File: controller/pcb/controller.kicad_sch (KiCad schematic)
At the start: 22 parts, among them SW1 SW_Push, SW2 SW_Push, SW3 SW_Push, SW4 SW_Push, U1 COM-09032, U2 COM-09032, U3 NRF24L01_Breakout, U4 ESP32C3-SUPERMINI, U5 74HC148

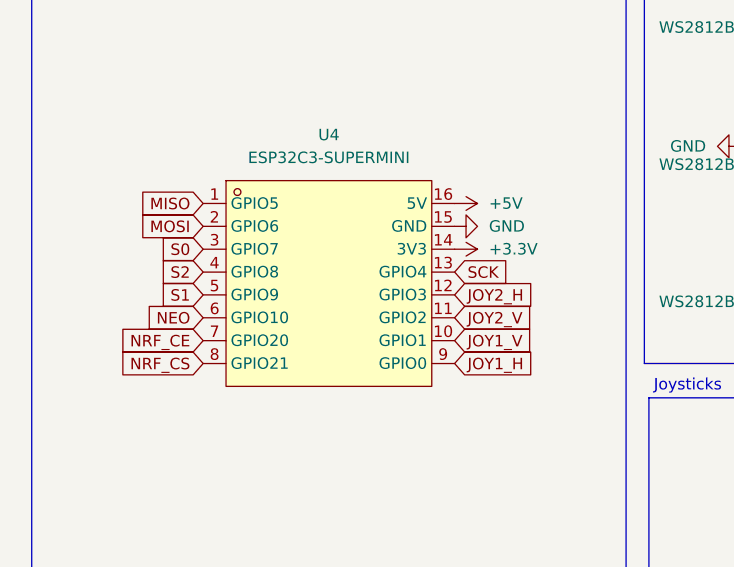
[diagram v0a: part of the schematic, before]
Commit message: [firmware] add v202 protocl and nrf24 driver code
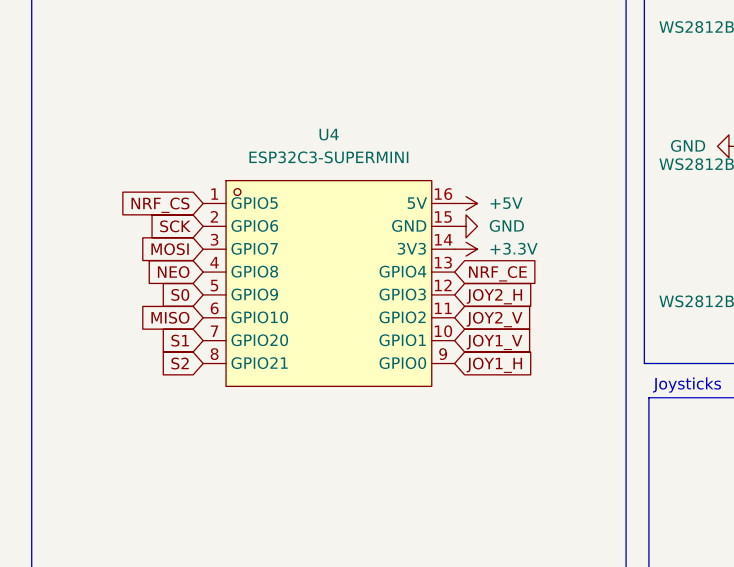
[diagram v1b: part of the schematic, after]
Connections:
- net MISO: now also U4.6 (GPIO10); no longer U4.1 (GPIO5)
- net MOSI: now also U4.3 (GPIO7); no longer U4.2 (GPIO6)
- net NEO: now also U4.4 (GPIO8); no longer U4.6 (GPIO10)
- net NRF_CE: now also U4.13 (GPIO4); no longer U4.7 (GPIO20)
- net NRF_CS: now also U4.1 (GPIO5); no longer U4.8 (GPIO21)
- net S0: now also U4.5 (GPIO9); no longer U4.3 (GPIO7)
- net S1: now also U4.7 (GPIO20); no longer U4.5 (GPIO9)
- net S2: now also U4.8 (GPIO21); no longer U4.4 (GPIO8)
- net SCK: now also U4.2 (GPIO6); no longer U4.13 (GPIO4)

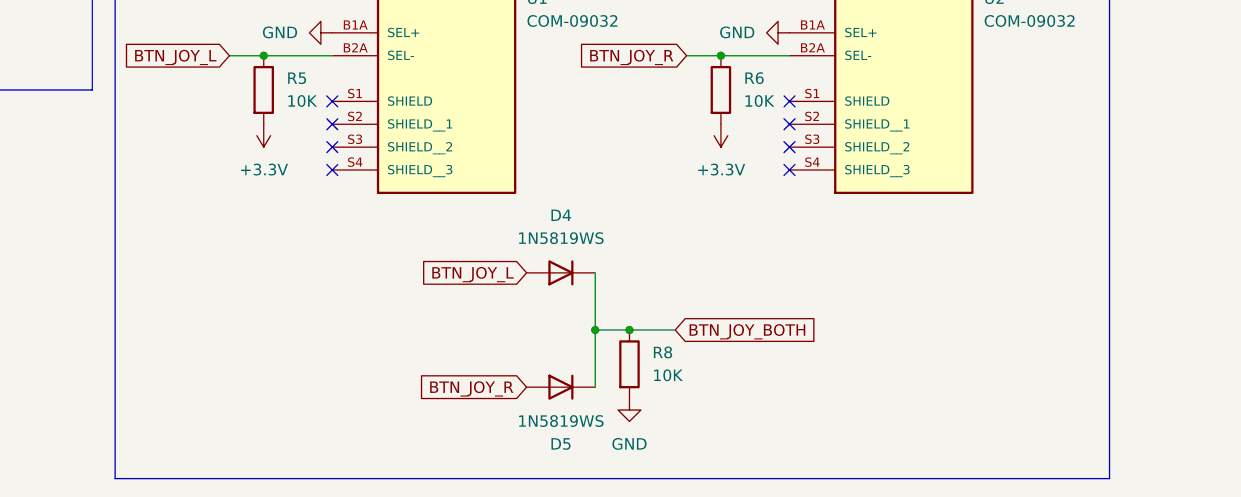
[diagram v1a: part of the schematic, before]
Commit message: [controller] add smoothing caps to ADC lines
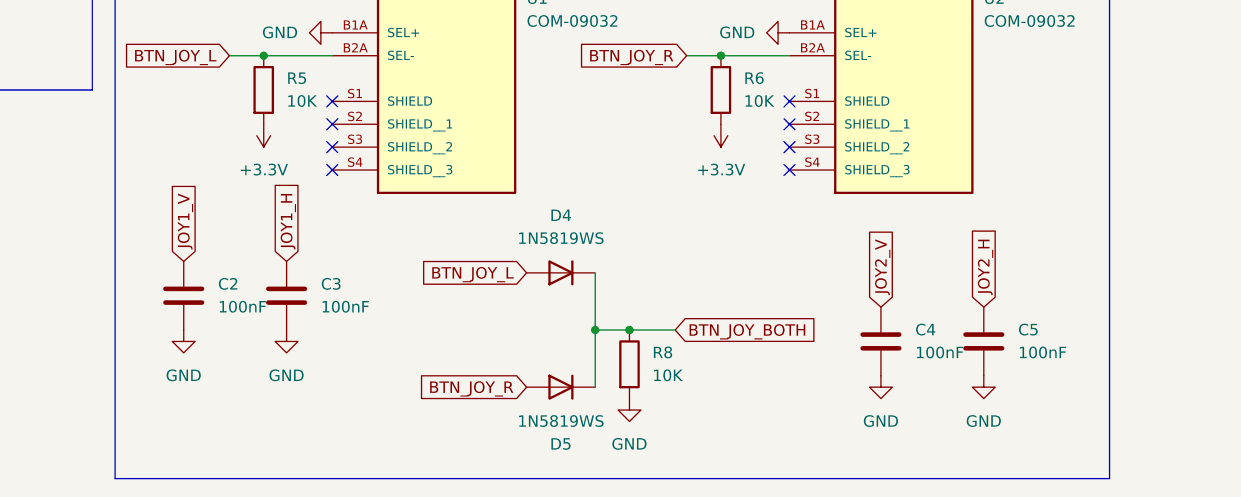
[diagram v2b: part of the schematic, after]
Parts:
- added C2, C3, C4, C5: 100nF, Capacitor_SMD:C_0805_2012Metric, symbol Device:C
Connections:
- net GND: now also C2.2, C3.2, C4.2, C5.2
- net JOY1_H: now also C3.1
- net JOY1_V: now also C2.1
- net JOY2_H: now also C5.1
- net JOY2_V: now also C4.1

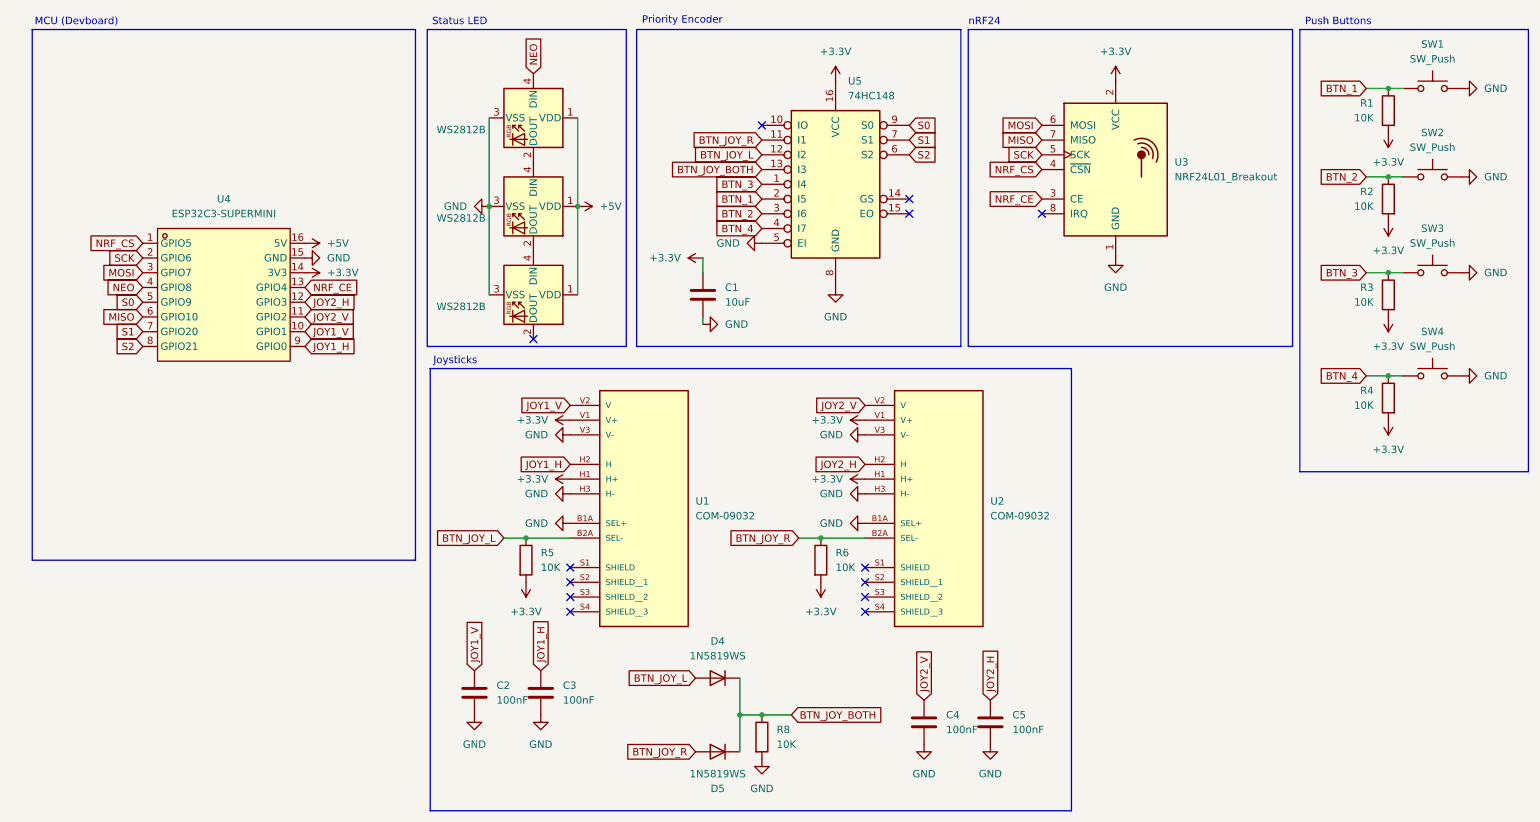
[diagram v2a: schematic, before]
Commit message: [controller] use higher quality external ADC
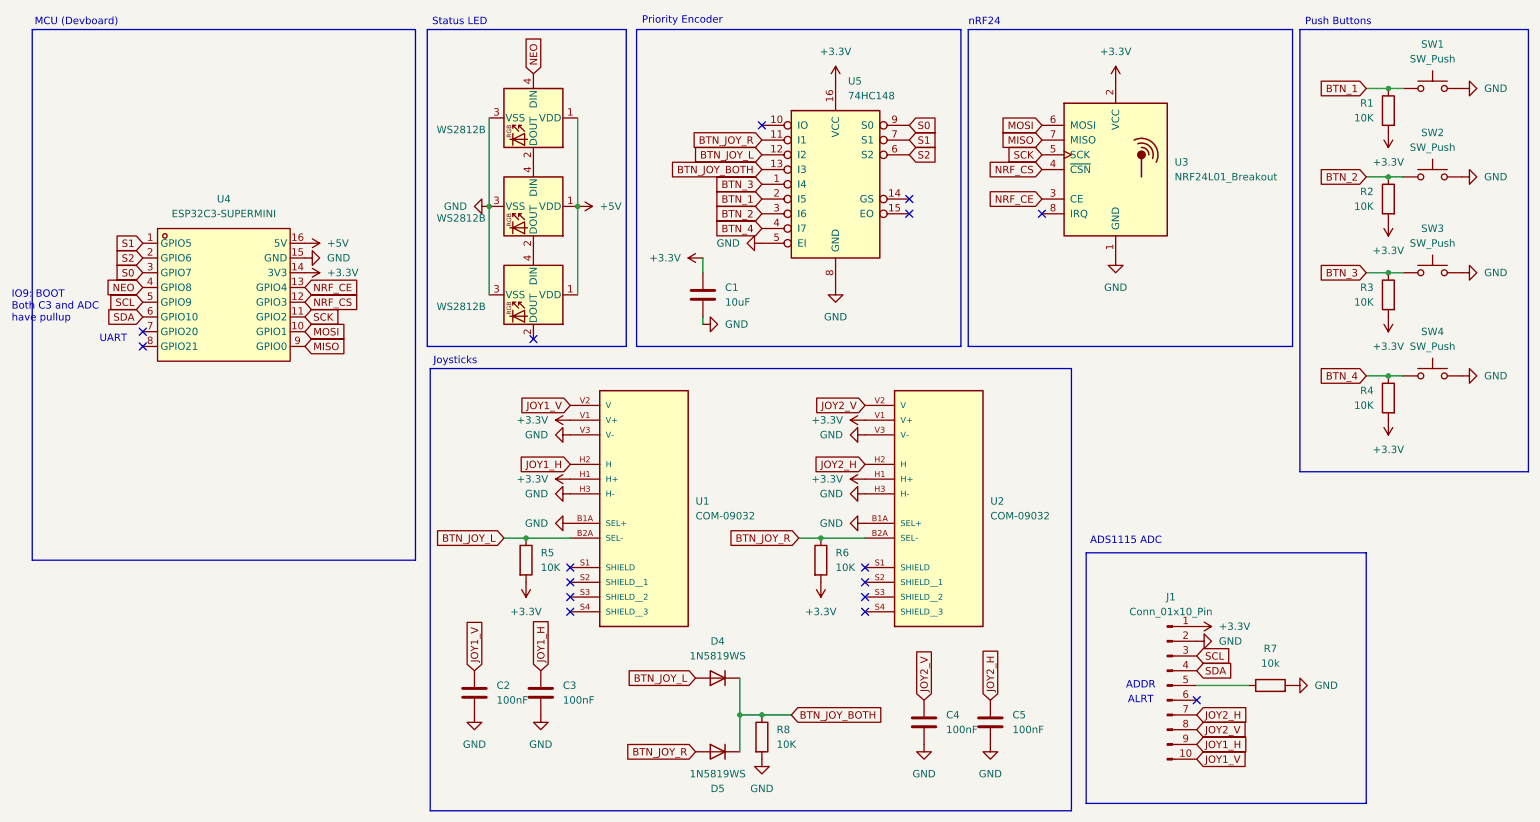
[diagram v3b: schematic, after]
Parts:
- added J1: Conn_01x10_Pin, Connector_PinHeader_2.54mm:PinHeader_1x10_P2.54mm_Vertical, symbol Connector:Conn_01x10_Pin
- added R7: 10k, Resistor_SMD:R_0805_2012Metric, symbol Device:R
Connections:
- net +3.3V: now also J1.1 (Pin_1)
- net GND: now also J1.2 (Pin_2), R7.2
- net JOY1_H: now also J1.9 (Pin_9); no longer U4.9 (GPIO0)
- net JOY1_V: now also J1.10 (Pin_10); no longer U4.10 (GPIO1)
- net JOY2_H: now also J1.7 (Pin_7); no longer U4.12 (GPIO3)
- net JOY2_V: now also J1.8 (Pin_8); no longer U4.11 (GPIO2)
- net MISO: now also U4.9 (GPIO0); no longer U4.6 (GPIO10)
- net MOSI: now also U4.10 (GPIO1); no longer U4.3 (GPIO7)
- net NRF_CS: now also U4.12 (GPIO3); no longer U4.1 (GPIO5)
- net S0: now also U4.3 (GPIO7); no longer U4.5 (GPIO9)
- net S1: now also U4.1 (GPIO5); no longer U4.7 (GPIO20)
- net S2: now also U4.2 (GPIO6); no longer U4.8 (GPIO21)
- net SCK: now also U4.11 (GPIO2); no longer U4.2 (GPIO6)
- new net: J1.5 (Pin_5), R7.1
- new net SCL: J1.3 (Pin_3), U4.5 (GPIO9)
- new net SDA: J1.4 (Pin_4), U4.6 (GPIO10)
- no-connect marks 13 -> 16
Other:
- note added: "ADDR"
- note added: "ADS1115 ADC"
- note added: "ALRT"
- note added: "IO9: BOOT Both C3 and ADC have pullup"
- note added: "UART"

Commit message: [controller] finish firmware, implement better ADC sampling w/ interrupt
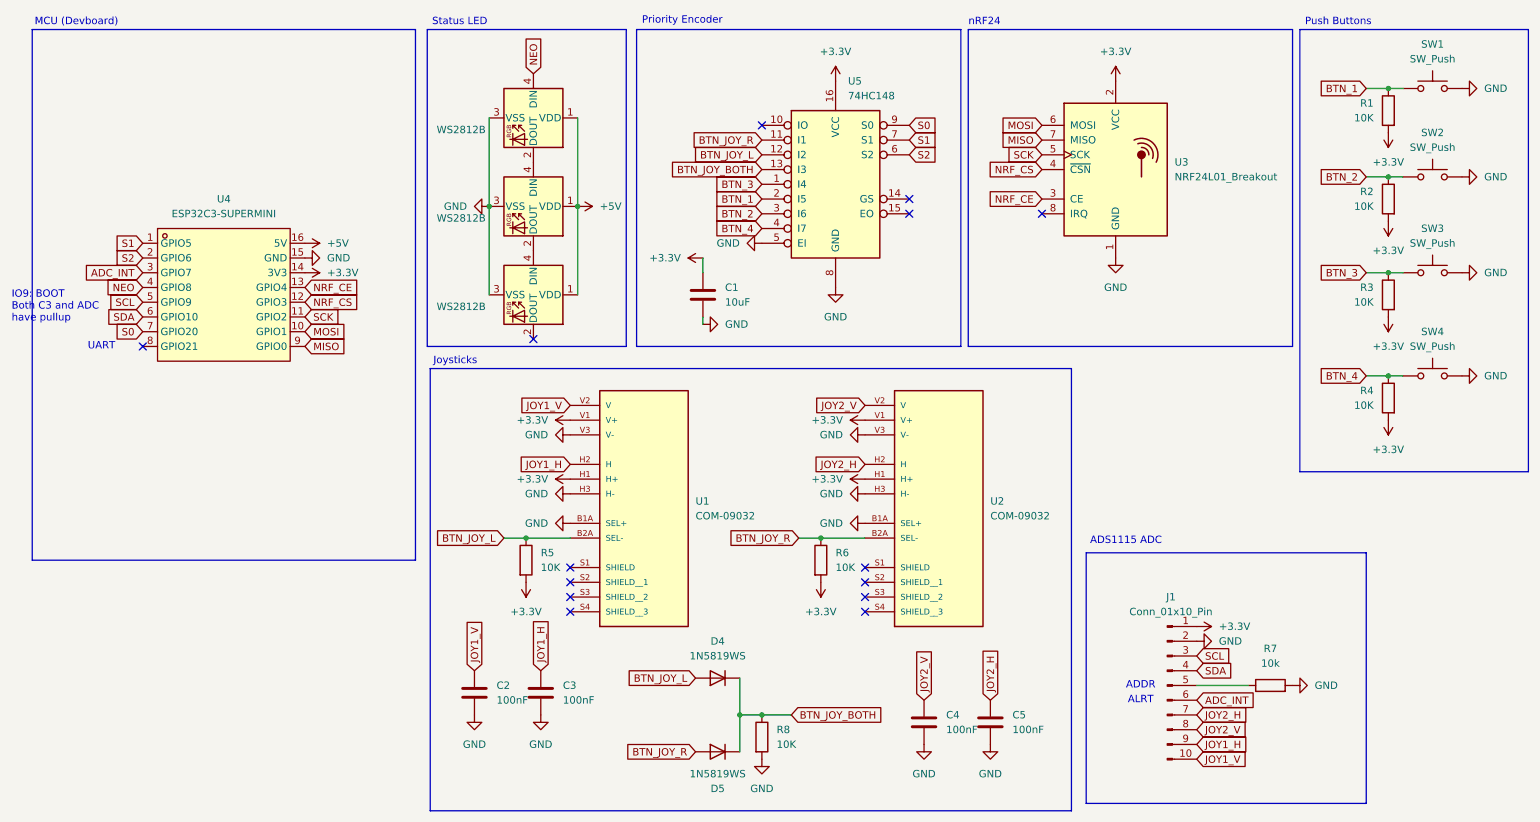
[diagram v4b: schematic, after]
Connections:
- net S0: now also U4.7 (GPIO20); no longer U4.3 (GPIO7)
- net ADC_INT: now reaches J1.6 (Pin_6)
- net ADC_INT: now also U4.3 (GPIO7)
- no-connect marks 16 -> 14
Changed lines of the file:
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@@
 	(text "UART"
 		(exclude_from_sim no)
-		(at 27.94 69.85 0)
+		(at 25.908 71.12 0)
 		(effects
 			(font
@@
 	)
 	(no_connect
-		(at 33.02 68.58)
-	)
-	(no_connect
 		(at 106.68 109.22)
 	)
@@
 	)
 	(no_connect
-		(at 214.63 132.08)
-	)
-	(no_connect
 		(at 157.48 116.84)
 	)
@@
 		)
 	)
+	(global_label "S0"
+		(shape input)
+		(at 33.02 68.58 180)
+		(fields_autoplaced yes)
+		(effects
+			(font
+				(size 1.27 1.27)
+			)
+			(justify right)
+		)
+		(property "Intersheetrefs" "${INTERSHEET_REFS}"
+			(at 27.6158 68.58 0)
+			(effects
+				(font
+					(size 1.27 1.27)
+				)
+				(justify right)
+				(hide yes)
+			)
+		)
+	)
 	(global_label "BTN_JOY_L"
 		(shape input)
@@
 		)
 	)
+	(global_label "ADC_INT"
+		(shape input)
+		(at 214.63 132.08 0)
+		(fields_autoplaced yes)
+		(effects
+			(font
+				(size 1.27 1.27)
+			)
+			(justify left)
+		)
+		(property "Intersheetrefs" "${INTERSHEET_REFS}"
+			(at 225.1143 132.08 0)
+			(effects
+				(font
+					(size 1.27 1.27)
+				)
+				(justify left)
+				(hide yes)
+			)
+		)
+	)
 	(global_label "BTN_JOY_BOTH"
 		(shape input)
@@
 		)
 	)
+	(global_label "S2"
+		(shape input)
+		(at 33.02 55.88 180)
+		(fields_autoplaced yes)
+		(effects
+			(font
+				(size 1.27 1.27)
+			)
+			(justify right)
+		)
+		(property "Intersheetrefs" "${INTERSHEET_REFS}"
+			(at 27.6158 55.88 0)
+			(effects
+				(font
+					(size 1.27 1.27)
+				)
+				(justify right)
+				(hide yes)
+			)
+		)
+	)
 	(global_label "JOY2_V"
 		(shape input)
@@
 		)
 	)
-	(global_label "S0"
+	(global_label "BTN_1"
+		(shape input)
+		(at 139.7 45.72 180)
+		(fields_autoplaced yes)
+		(effects
+			(font
+				(size 1.27 1.27)
+			)
+			(justify right)
+		)
+		(property "Intersheetrefs" "${INTERSHEET_REFS}"
+			(at 130.9696 45.72 0)
+			(effects
+				(font
+					(size 1.27 1.27)
+				)
+				(justify right)
+				(hide yes)
+			)
+		)
+	)
+	(global_label "NRF_CS"
+		(shape input)
+		(at 187.96 40.64 180)
+		(fields_autoplaced yes)
+		(effects
+			(font
+				(size 1.27 1.27)
+			)
+			(justify right)
+		)
+		(property "Intersheetrefs" "${INTERSHEET_REFS}"
+			(at 177.8386 40.64 0)
+			(effects
+				(font
+					(size 1.27 1.27)
+				)
+				(justify right)
+				(hide yes)
+			)
+		)
+	)
+	(global_label "JOY1_V"
+		(shape input)
+		(at 90.17 127 90)
+		(fields_autoplaced yes)
+		(effects
+			(font
+				(size 1.27 1.27)
+			)
+			(justify left)
+		)
+		(property "Intersheetrefs" "${INTERSHEET_REFS}"
+			(at 90.17 117.3624 90)
+			(effects
+				(font
+					(size 1.27 1.27)
+				)
+				(justify left)
+				(hide yes)
+			)
+		)
+	)
+	(global_label "MISO"
+		(shape input)
+		(at 60.96 71.12 0)
+		(fields_autoplaced yes)
+		(effects
+			(font
+				(size 1.27 1.27)
+			)
+			(justify left)
+		)
+		(property "Intersheetrefs" "${INTERSHEET_REFS}"
+			(at 68.5414 71.12 0)
+			(effects
+				(font
+					(size 1.27 1.27)
+				)
+				(justify left)
+				(hide yes)
+			)
+		)
+	)
+	(global_label "BTN_JOY_R"
+		(shape input)
+		(at 128.27 140.97 180)
+		(fields_autoplaced yes)
+		(effects
+			(font
+				(size 1.27 1.27)
+			)
+			(justify right)
+		)
+		(property "Intersheetrefs" "${INTERSHEET_REFS}"
+			(at 115.1248 140.97 0)
+			(effects
+				(font
+					(size 1.27 1.27)
+				)
+				(justify right)
+				(hide yes)
+			)
+		)
+	)
+	(global_label "BTN_2"
+		(shape input)
+		(at 139.7 48.26 180)
+		(fields_autoplaced yes)
+		(effects
+			(font
+				(size 1.27 1.27)
+			)
+			(justify right)
+		)
+		(property "Intersheetrefs" "${INTERSHEET_REFS}"
+			(at 130.9696 48.26 0)
+			(effects
+				(font
+					(size 1.27 1.27)
+				)
+				(justify right)
+				(hide yes)
+			)
+		)
+	)
+	(global_label "BTN_3"
+		(shape input)
+		(at 243.84 58.42 180)
+		(fields_autoplaced yes)
+		(effects
+			(font
+				(size 1.27 1.27)
+			)
+			(justify right)
+		)
+		(property "Intersheetrefs" "${INTERSHEET_REFS}"
+			(at 235.1096 58.42 0)
+			(effects
+				(font
+					(size 1.27 1.27)
+				)
+				(justify right)
+				(hide yes)
+			)
+		)
+	)
+	(global_label "ADC_INT"
 		(shape input)
 		(at 33.02 58.42 180)
@@
 		)
 		(property "Intersheetrefs" "${INTERSHEET_REFS}"
-			(at 27.6158 58.42 0)
-			(effects
-				(font
-					(size 1.27 1.27)
-				)
-				(justify right)
-				(hide yes)
-			)
-		)
-	)
-	(global_label "BTN_1"
-		(shape input)
-		(at 139.7 45.72 180)
-		(fields_autoplaced yes)
-		(effects
-			(font
-				(size 1.27 1.27)
-			)
-			(justify right)
-		)
-		(property "Intersheetrefs" "${INTERSHEET_REFS}"
-			(at 130.9696 45.72 0)
-			(effects
-				(font
-					(size 1.27 1.27)
-				)
-				(justify right)
-				(hide yes)
-			)
-		)
-	)
-	(global_label "NRF_CS"
-		(shape input)
-		(at 187.96 40.64 180)
-		(fields_autoplaced yes)
-		(effects
-			(font
-				(size 1.27 1.27)
-			)
-			(justify right)
-		)
-		(property "Intersheetrefs" "${INTERSHEET_REFS}"
-			(at 177.8386 40.64 0)
-			(effects
-				(font
-					(size 1.27 1.27)
-				)
-				(justify right)
-				(hide yes)
-			)
-		)
-	)
-	(global_label "S2"
-		(shape input)
-		(at 33.02 55.88 180)
-		(fields_autoplaced yes)
-		(effects
-			(font
-				(size 1.27 1.27)
-			)
-			(justify right)
-		)
-		(property "Intersheetrefs" "${INTERSHEET_REFS}"
-			(at 27.6158 55.88 0)
-			(effects
-				(font
-					(size 1.27 1.27)
-				)
-				(justify right)
-				(hide yes)
-			)
-		)
-	)
-	(global_label "JOY1_V"
-		(shape input)
-		(at 90.17 127 90)
-		(fields_autoplaced yes)
-		(effects
-			(font
-				(size 1.27 1.27)
-			)
-			(justify left)
-		)
-		(property "Intersheetrefs" "${INTERSHEET_REFS}"
-			(at 90.17 117.3624 90)
-			(effects
-				(font
-					(size 1.27 1.27)
-				)
-				(justify left)
-				(hide yes)
-			)
-		)
-	)
-	(global_label "MISO"
-		(shape input)
-		(at 60.96 71.12 0)
-		(fields_autoplaced yes)
-		(effects
-			(font
-				(size 1.27 1.27)
-			)
-			(justify left)
-		)
-		(property "Intersheetrefs" "${INTERSHEET_REFS}"
-			(at 68.5414 71.12 0)
-			(effects
-				(font
-					(size 1.27 1.27)
-				)
-				(justify left)
-				(hide yes)
-			)
-		)
-	)
-	(global_label "BTN_JOY_R"
-		(shape input)
-		(at 128.27 140.97 180)
-		(fields_autoplaced yes)
-		(effects
-			(font
-				(size 1.27 1.27)
-			)
-			(justify right)
-		)
-		(property "Intersheetrefs" "${INTERSHEET_REFS}"
-			(at 115.1248 140.97 0)
-			(effects
-				(font
-					(size 1.27 1.27)
-				)
-				(justify right)
-				(hide yes)
-			)
-		)
-	)
-	(global_label "BTN_2"
-		(shape input)
-		(at 139.7 48.26 180)
-		(fields_autoplaced yes)
-		(effects
-			(font
-				(size 1.27 1.27)
-			)
-			(justify right)
-		)
-		(property "Intersheetrefs" "${INTERSHEET_REFS}"
-			(at 130.9696 48.26 0)
-			(effects
-				(font
-					(size 1.27 1.27)
-				)
-				(justify right)
-				(hide yes)
-			)
-		)
-	)
-	(global_label "BTN_3"
-		(shape input)
-		(at 243.84 58.42 180)
-		(fields_autoplaced yes)
-		(effects
-			(font
-				(size 1.27 1.27)
-			)
-			(justify right)
-		)
-		(property "Intersheetrefs" "${INTERSHEET_REFS}"
-			(at 235.1096 58.42 0)
-			(effects
-				(font
+			(at 22.5357 58.42 0)
+			(effects
+				(font

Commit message: [bom] change battery and [controller] add button 3d files
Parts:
- SW1, SW2, SW3, SW4: footprint Button_Switch_THT:SW_PUSH-12mm -> stuff:SW_PUSH-12mm
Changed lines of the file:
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@@
 			)
 		)
-		(property "Footprint" "Button_Switch_THT:SW_PUSH-12mm"
+		(property "Footprint" "stuff:SW_PUSH-12mm"
 			(at 255.27 71.12 0)
 			(effects
@@
 			)
 		)
-		(property "Footprint" "Button_Switch_THT:SW_PUSH-12mm"
+		(property "Footprint" "stuff:SW_PUSH-12mm"
 			(at 255.27 36.83 0)
 			(effects
@@
 			)
 		)
-		(property "Footprint" "Button_Switch_THT:SW_PUSH-12mm"
+		(property "Footprint" "stuff:SW_PUSH-12mm"
 			(at 255.27 21.59 0)
 			(effects
@@
 			)
 		)
-		(property "Footprint" "Button_Switch_THT:SW_PUSH-12mm"
+		(property "Footprint" "stuff:SW_PUSH-12mm"
 			(at 255.27 53.34 0)
 			(effects
